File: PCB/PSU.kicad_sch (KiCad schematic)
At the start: 47 parts, among them Q2 BSS138BKS, U12 TPS61040DBV, U13 INA180A4, U14 TPS259533, U6 AP2127K-ADJ, U7 XC6206P332MR, U9 TPS259533

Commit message: Initial V2.1 update.
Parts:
- added R43: 10k, Resistor_SMD:R_0402_1005Metric, symbol Device:R_Small
- R16: value 1M -> 10k; LCSC C26083 -> C25744; now not fitted
- R17: value 330k -> 10k; LCSC C25778 -> C25744
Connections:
- net +5V: now also R43.1
- net RGB_EN: now also R43.2
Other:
- moved on the sheet: C45

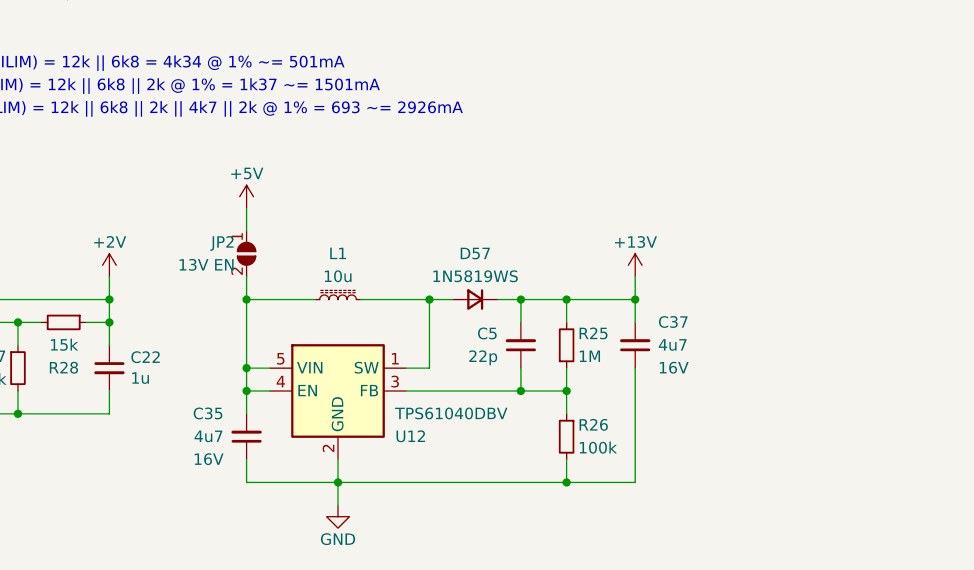
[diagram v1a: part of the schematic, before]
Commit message: Routed 13V EN pin to the MCU. Removed solder jumper.
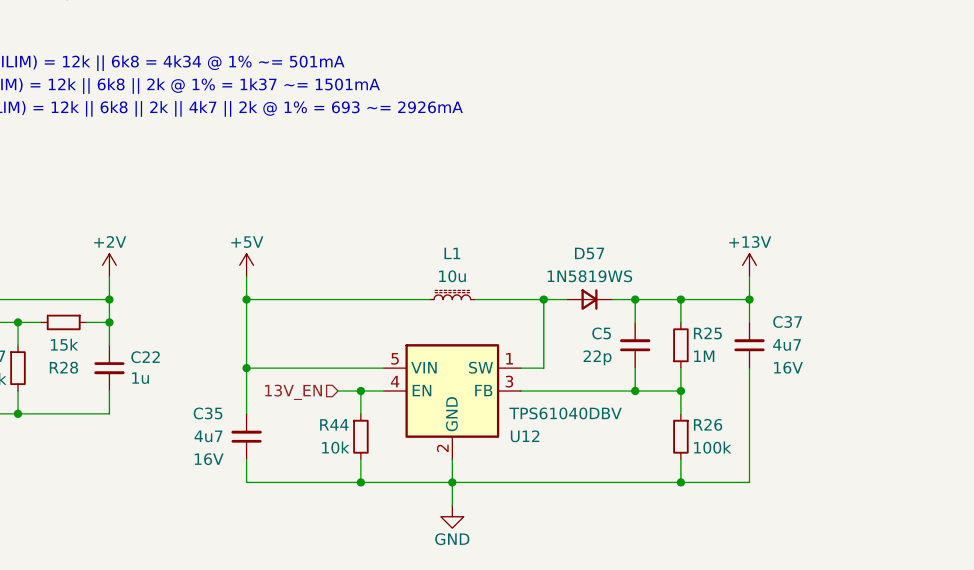
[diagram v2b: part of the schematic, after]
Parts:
- removed JP2: 13V EN, Honeydew:SolderJumper-2_P1.2mm_Open_Pad1.0x1.0mm, symbol Honeydew:SolderJumper_2_Open
- added R44: 10k, Resistor_SMD:R_0402_1005Metric, symbol Device:R_Small
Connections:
- net +5V: now also C35.2, L1.2, U12.5 (VIN)
- net GND: now also R44.2
- new net 13V_EN: R44.1, U12.4 (EN)
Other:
- moved on the sheet: C37, C5, D57, L1, R25, R26, U12

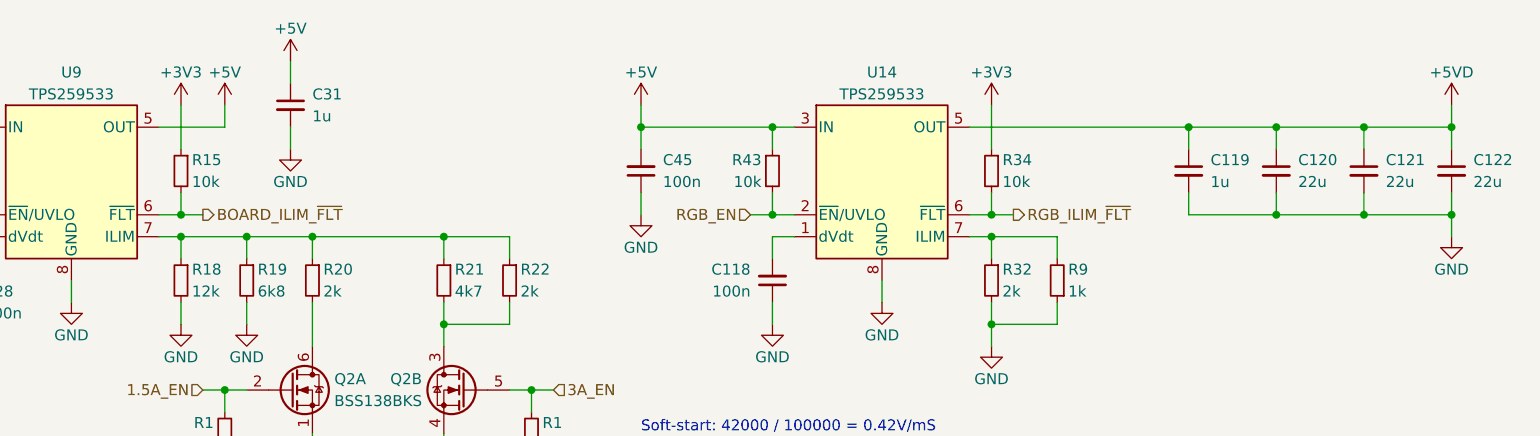
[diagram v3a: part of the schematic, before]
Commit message: 14/07/2023 update
Replaced 1N4148 switch diodes with BAV70. Replaced switch footprints with combination MX/Choc hotswap footprints. Replaced flash IC with much smaller version. Removed buttons and USB-C port and replaced it with an FFC connector for [Galia](https://github.com/Ariamelon/Galia) (a USB-C daughterboard designed specifically for the Honeydew). Added case STEP file and renders.
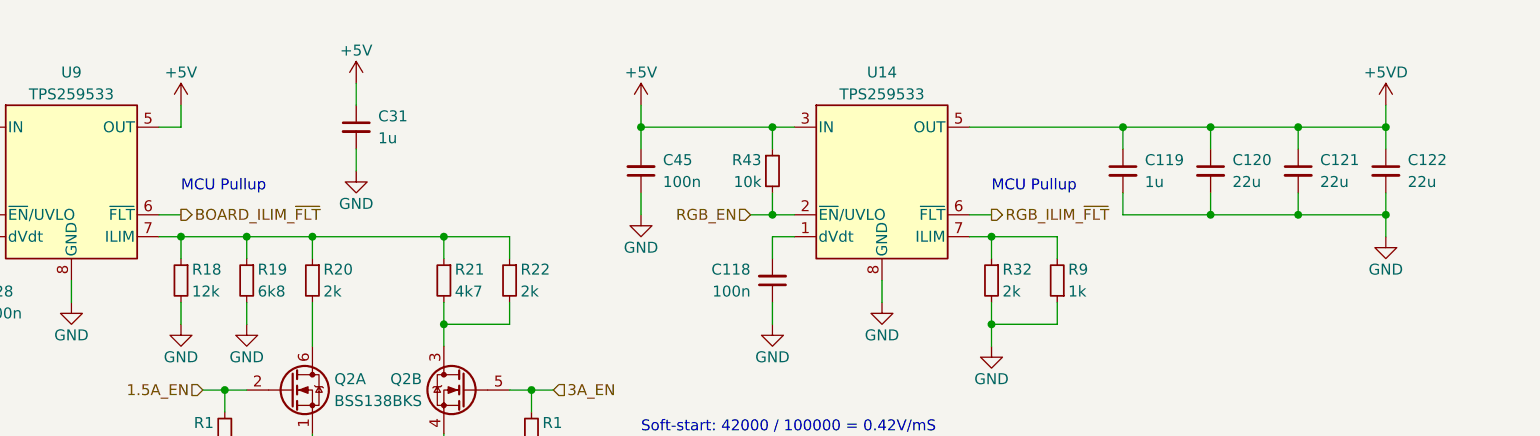
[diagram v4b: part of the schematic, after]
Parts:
- removed R15, R34: 10k, Resistor_SMD:R_0402_1005Metric, symbol Device:R_Small
- C119, C21, C22, C3, C31, C4: footprint Capacitor_SMD:C_0603_1608Metric -> Capacitor_SMD:C_0402_1005Metric; LCSC C15849 -> C52923; Voltage 50V -> 25V
- U13: LCSC (none) -> C188337
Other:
- note added: "MCU Pullup"
- moved on the sheet: C119, C120, C121, C122, C31
